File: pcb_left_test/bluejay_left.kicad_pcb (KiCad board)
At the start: 2 copper layers, 147 x 140.5 mm, 81 parts, among them J1 SJ-43514, U1 ATmega328P-PU, Y1 16MHz

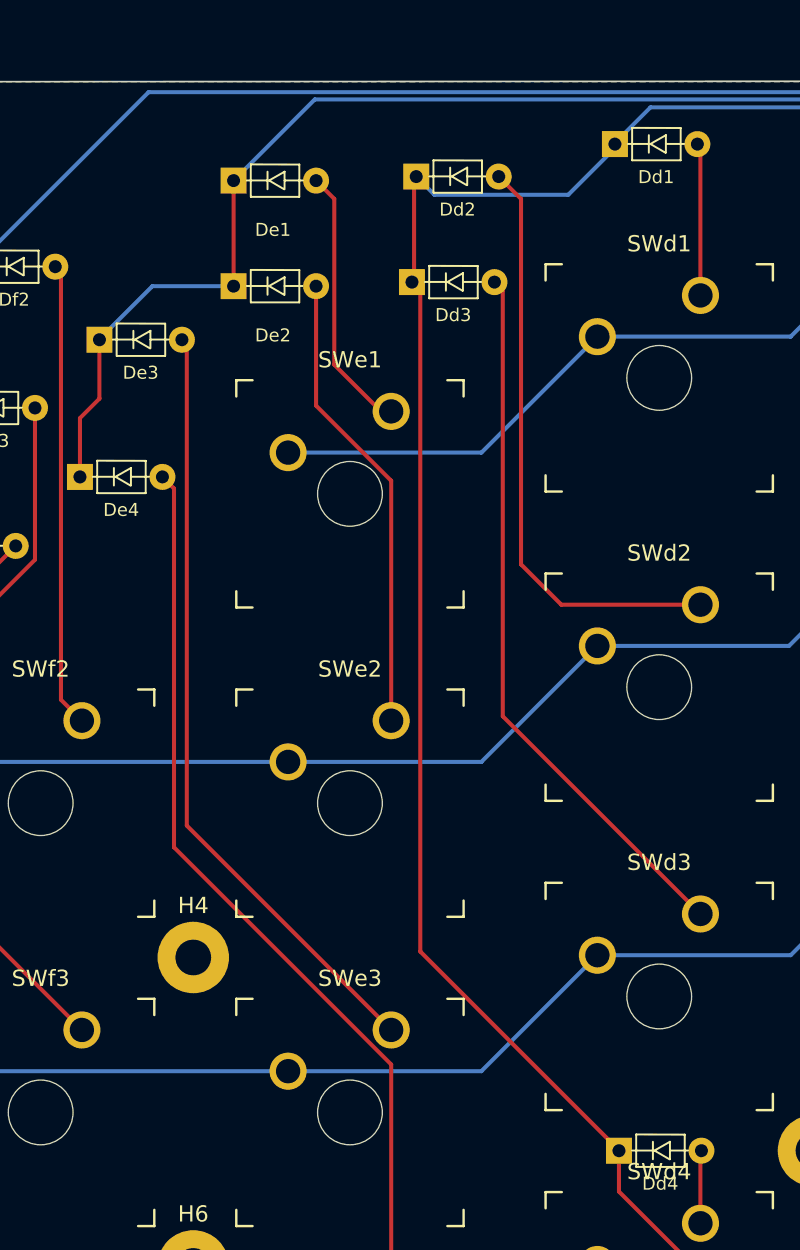
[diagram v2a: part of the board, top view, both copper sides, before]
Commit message: Fine tune placement of diodes
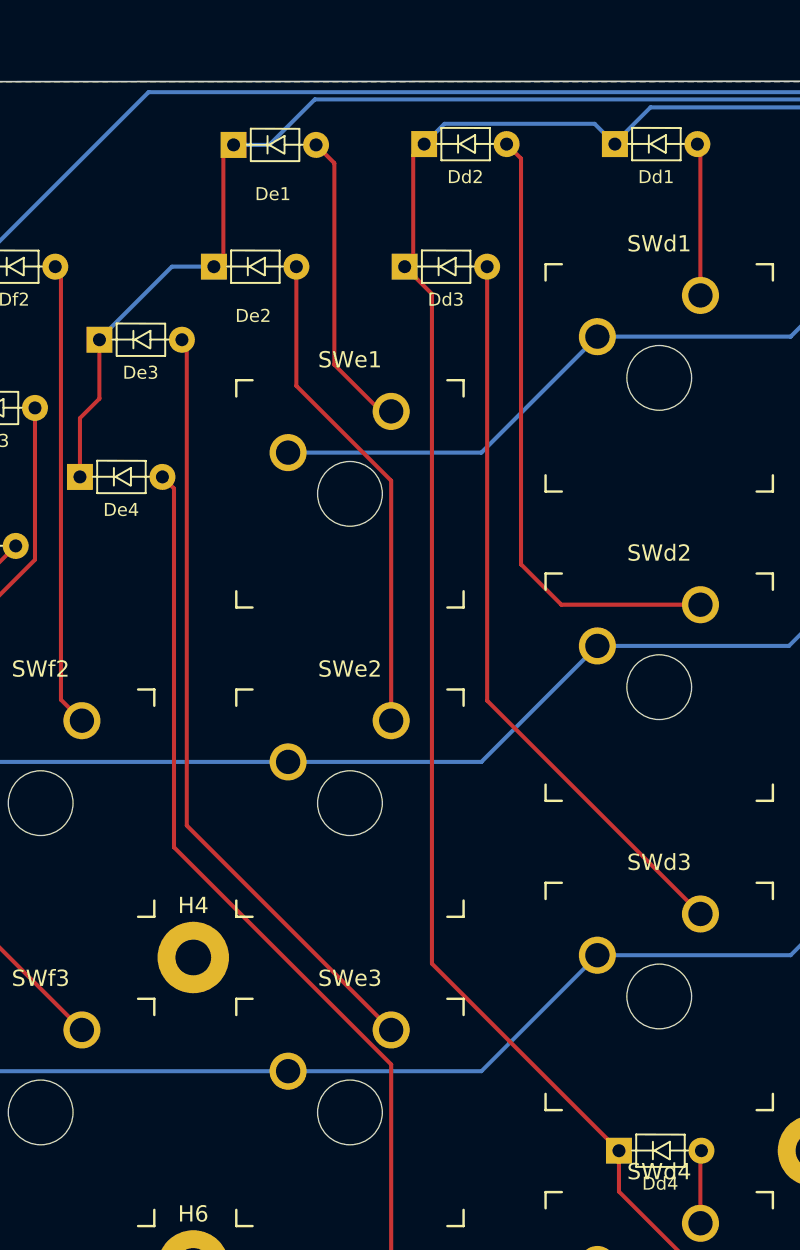
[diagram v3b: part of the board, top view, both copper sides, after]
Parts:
- moved De1 2.20 mm to (-65.6, -52.5)
- moved Dd2 2.06 mm to (-53.9, -52.5)
- moved De2 1.71 mm to (-66.8, -45.0)
- moved Dd3 1.05 mm to (-55.0, -45.0)
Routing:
- net Net-(De1-Pad2): track 16.5 -> 18.7 mm
- net Net-(Dd2-Pad2): track 36.5 -> 38.3 mm
- net Net-(De2-Pad2): track 28.7 -> 30.4 mm
- net /colD: track 228.3 -> 229.5 mm
- net Net-(Dd3-Pad2): track 44.2 -> 45.3 mm
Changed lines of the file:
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@@
   )
   (footprint "BlueJay footprints:D_DO-35_SOD27_P5.08mm_Horizontal" (layer "F.Cu")
-    (at -65.5875 -43.75)
+    (at -66.8 -44.95)
     (descr "Diode, DO-35_SOD27 series, Axial, Horizontal, pin pitch=7.62mm, , length*diameter=4*2mm^2, , http://www.diodes.com/_files/packages/DO-35.pdf")
     (tags "Diode DO-35_SOD27 series Axial Horizontal pin pitch 7.62mm  length 4mm diameter 2mm")
@@
   )
   (footprint "BlueJay footprints:D_DO-35_SOD27_P5.08mm_Horizontal" (layer "F.Cu")
-    (at -65.5875 -50.25)
+    (at -65.5875 -52.45)
     (descr "Diode, DO-35_SOD27 series, Axial, Horizontal, pin pitch=7.62mm, , length*diameter=4*2mm^2, , http://www.diodes.com/_files/packages/DO-35.pdf")
     (tags "Diode DO-35_SOD27 series Axial Horizontal pin pitch 7.62mm  length 4mm diameter 2mm")
@@
   )
   (footprint "BlueJay footprints:D_DO-35_SOD27_P5.08mm_Horizontal" (layer "F.Cu")
-    (at -54.3375 -50.5)
+    (at -53.85 -52.5)
     (descr "Diode, DO-35_SOD27 series, Axial, Horizontal, pin pitch=7.62mm, , length*diameter=4*2mm^2, , http://www.diodes.com/_files/packages/DO-35.pdf")
     (tags "Diode DO-35_SOD27 series Axial Horizontal pin pitch 7.62mm  length 4mm diameter 2mm")
@@
   )
   (footprint "BlueJay footprints:D_DO-35_SOD27_P5.08mm_Horizontal" (layer "F.Cu")
-    (at -54.6 -44)
+    (at -55.05 -44.95)
     (descr "Diode, DO-35_SOD27 series, Axial, Horizontal, pin pitch=7.62mm, , length*diameter=4*2mm^2, , http://www.diodes.com/_files/packages/DO-35.pdf")
     (tags "Diode DO-35_SOD27 series Axial Horizontal pin pitch 7.62mm  length 4mm diameter 2mm")
@@
   (segment (start -40.58 12.02) (end -40.58 9.5) (width 0.25) (layer "F.Cu") (net 23))
   (segment (start -22.1175 28.4) (end -24.2 28.4) (width 0.25) (layer "F.Cu") (net 23))
+  (segment (start -52.1 -43.27) (end -53.78 -44.95) (width 0.25) (layer "F.Cu") (net 23))
   (segment (start -24.2 28.4) (end -40.58 12.02) (width 0.25) (layer "F.Cu") (net 23))
-  (segment (start -40.58 9.47) (end -52.8175 -2.7675) (width 0.25) (layer "F.Cu") (net 23))
-  (segment (start -52.8175 -2.7675) (end -52.8175 -43.4875) (width 0.25) (layer "F.Cu") (net 23))
-  (segment (start -53.2 -50.3675) (end -53.0675 -50.5) (width 0.25) (layer "F.Cu") (net 23))
-  (segment (start -52.8175 -43.4875) (end -53.33 -44) (width 0.25) (layer "F.Cu") (net 23))
-  (segment (start -53.33 -44) (end -53.2 -44.13) (width 0.25) (layer "F.Cu") (net 23))
+  (segment (start -40.58 9.5) (end -52.1 -2.02) (width 0.25) (layer "F.Cu") (net 23))
+  (segment (start -52.1 -2.02) (end -52.1 -43.27) (width 0.25) (layer "F.Cu") (net 23))
+  (segment (start -53.25 -45.48) (end -53.25 -51.83) (width 0.25) (layer "F.Cu") (net 23))
+  (segment (start -53.78 -44.95) (end -53.25 -45.48) (width 0.25) (layer "F.Cu") (net 23))
   (segment (start 55.2755 -19.1418) (end 53.5512 -17.4175) (width 0.25) (layer "F.Cu") (net 23))
-  (segment (start -40.58 9.5) (end -40.58 9.47) (width 0.25) (layer "F.Cu") (net 23))
-  (segment (start -53.2 -44.13) (end -53.2 -50.3675) (width 0.25) (layer "F.Cu") (net 23))
+  (segment (start -53.25 -51.83) (end -52.58 -52.5) (width 0.25) (layer "F.Cu") (net 23))
   (via (at 55.2755 -30.550989) (size 0.8) (drill 0.4) (layers "F.Cu" "B.Cu") (net 23))
+  (segment (start -51.33 -53.75) (end -42.08 -53.75) (width 0.25) (layer "B.Cu") (net 23))
   (segment (start 54.726489 -31.1) (end 55.2755 -30.550989) (width 0.25) (layer "B.Cu") (net 23))
+  (segment (start -42.08 -53.75) (end -40.83 -52.5) (width 0.25) (layer "B.Cu") (net 23))
   (segment (start 38.2 -31.1) (end 54.726489 -31.1) (width 0.25) (layer "B.Cu") (net 23))
-  (segment (start -51.942989 -49.375489) (end -43.704511 -49.375489) (width 0.25) (layer "B.Cu") (net 23))
   (segment (start -38.635718 -54.764282) (end 14.535718 -54.764282) (width 0.25) (layer "B.Cu") (net 23))
-  (segment (start -43.704511 -49.375489) (end -40.83 -52.25) (width 0.25) (layer "B.Cu") (net 23))
+  (segment (start -52.58 -52.5) (end -51.33 -53.75) (width 0.25) (layer "B.Cu") (net 23))
   (segment (start -40.83 -52.57) (end -38.635718 -54.764282) (width 0.25) (layer "B.Cu") (net 23))
   (segment (start 14.535718 -54.764282) (end 38.2 -31.1) (width 0.25) (layer "B.Cu") (net 23))
-  (segment (start -40.83 -52.25) (end -40.83 -52.5) (width 0.25) (layer "B.Cu") (net 23))
-  (segment (start -53.0675 -50.5) (end -51.942989 -49.375489) (width 0.25) (layer "B.Cu") (net 23))
   (segment (start -40.83 -52.5) (end -40.83 -52.57) (width 0.25) (layer "B.Cu") (net 23))
   (segment (start -35.56 -52.31) (end -35.75 -52.5) (width 0.25) (layer "F.Cu") (net 24))
   (segment (start -35.56 -43.18) (end -35.56 -52.31) (width 0.25) (layer "F.Cu") (net 24))
-  (segment (start -44.13 -24.13) (end -46.612989 -26.612989) (width 0.25) (layer "F.Cu") (net 25))
   (segment (start -35.56 -24.13) (end -44.13 -24.13) (width 0.25) (layer "F.Cu") (net 25))
-  (segment (start -46.612989 -26.612989) (end -46.612989 -49.125489) (width 0.25) (layer "F.Cu") (net 25))
-  (segment (start -46.612989 -49.125489) (end -47.9875 -50.5) (width 0.25) (layer "F.Cu") (net 25))
-  (segment (start -47.7375 -43.4875) (end -48.25 -44) (width 0.25) (layer "F.Cu") (net 26))
-  (segment (start -35.56 -5.08) (end -47.7375 -17.2575) (width 0.25) (layer "F.Cu") (net 26))
-  (segment (start -47.7375 -17.2575) (end -47.7375 -43.4875) (width 0.25) (layer "F.Cu") (net 26))
+  (segment (start -46.612989 -51.612989) (end -47.5 -52.5) (width 0.25) (layer "F.Cu") (net 25))
+  (segment (start -46.612989 -26.612989) (end -46.612989 -51.612989) (width 0.25) (layer "F.Cu") (net 25))
+  (segment (start -44.13 -24.13) (end -46.612989 -26.612989) (width 0.25) (layer "F.Cu") (net 25))
+  (segment (start -48.7 -18.22) (end -48.7 -44.95) (width 0.25) (layer "F.Cu") (net 26))
+  (segment (start -35.56 -5.08) (end -48.7 -18.22) (width 0.25) (layer "F.Cu") (net 26))
   (segment (start -35.56 13.97) (end -35.56 9.56) (width 0.25) (layer "F.Cu") (net 27))
   (segment (start -35.56 9.56) (end -35.5 9.5) (width 0.25) (layer "F.Cu") (net 27))
   (segment (start -6.985 40.1638) (end -6.985 38.4525) (width 0.25) (layer "F.Cu") (net 28))
   (segment (start -6.985 38.4525) (end -17.0375 28.4) (width 0.25) (layer "F.Cu") (net 28))
+  (segment (start -64.95 -45.53) (end -64.95 -51.8175) (width 0.25) (layer "F.Cu") (net 29))
   (segment (start 56 -31.243596) (end 56 -17.3263) (width 0.25) (layer "F.Cu") (net 29))
   (segment (start 56 -17.3263) (end 53.5512 -14.8775) (width 0.25) (layer "F.Cu") (net 29))
+  (segment (start -64.95 -51.8175) (end -64.3175 -52.45) (width 0.25) (layer "F.Cu") (net 29))
+  (segment (start -65.53 -44.95) (end -64.95 -45.53) (width 0.25) (layer "F.Cu") (net 29))
   (segment (start -73.78 -32) (end -73.78 -35.62) (width 0.25) (layer "F.Cu") (net 29))
-  (segment (start -64.3175 -43.75) (end -64.3175 -50.25) (width 0.25) (layer "F.Cu") (net 29))
   (segment (start 56.031904 -31.2755) (end 56 -31.243596) (width 0.25) (layer "F.Cu") (net 29))
   (segment (start -72.58 -36.82) (end -72.58 -40.45) (width 0.25) (layer "F.Cu") (net 29))
   (segment (start -73.78 -35.62) (end -72.58 -36.82) (width 0.25) (layer "F.Cu") (net 29))
   (via (at 56.031904 -31.2755) (size 0.8) (drill 0.4) (layers "F.Cu" "B.Cu") (net 29))
+  (segment (start -68.1175 -44.95) (end -65.53 -44.95) (width 0.25) (layer "B.Cu") (net 29))
   (segment (start -72.58 -40.45) (end -72.58 -40.4875) (width 0.25) (layer "B.Cu") (net 29))
-  (segment (start -72.58 -40.4875) (end -69.3175 -43.75) (width 0.25) (layer "B.Cu") (net 29))
-  (segment (start -69.3175 -43.75) (end -64.3175 -43.75) (width 0.25) (layer "B.Cu") (net 29))
-  (segment (start -64.3175 -50.25) (end -59.31702 -55.25048) (width 0.25) (layer "B.Cu") (net 29))
+  (segment (start -62.1175 -52.45) (end -59.31702 -55.25048) (width 0.25) (layer "B.Cu") (net 29))
+  (segment (start 14.713802 -55.25048) (end 38.164282 -31.8) (width 0.25) (layer "B.Cu") (net 29))
   (segment (start 55.507404 -31.8) (end 56.031904 -31.2755) (width 0.25) (layer "B.Cu") (net 29))
-  (segment (start 38.164282 -31.8) (end 55.507404 -31.8) (width 0.25) (layer "B.Cu") (net 29))
+  (segment (start -72.58 -40.4875) (end -68.1175 -44.95) (width 0.25) (layer "B.Cu") (net 29))
   (segment (start -59.31702 -55.25048) (end 14.713802 -55.25048) (width 0.25) (layer "B.Cu") (net 29))
-  (segment (start 14.713802 -55.25048) (end 38.164282 -31.8) (width 0.25) (layer "B.Cu") (net 29))
+  (segment (start -64.3175 -52.45) (end -62.1175 -52.45) (width 0.25) (layer "B.Cu") (net 29))
+  (segment (start 38.164282 -31.8) (end 55.507404 -31.8) (width 0.25) (layer "B.Cu") (net 29))
   (segment (start -54.61 -36.0363) (end -55.2363 -36.0363) (width 0.25) (layer "F.Cu") (net 30))
-  (segment (start -58.112989 -49.125489) (end -59.2375 -50.25) (width 0.25) (layer "F.Cu") (net 30))
-  (segment (start -58.112989 -38.912989) (end -58.112989 -49.125489) (width 0.25) (layer "F.Cu") (net 30))
+  (segment (start -58.112989 -38.912989) (end -58.112989 -51.325489) (width 0.25) (layer "F.Cu") (net 30))
   (segment (start -55.2363 -36.0363) (end -58.112989 -38.912989) (width 0.25) (layer "F.Cu") (net 30))
-  (segment (start -59.2375 -36.393254) (end -59.2375 -43.75) (width 0.25) (layer "F.Cu") (net 31))
-  (segment (start -54.61 -31.765754) (end -59.2375 -36.393254) (width 0.25) (layer "F.Cu") (net 31))
+  (segment (start -58.112989 -51.325489) (end -59.2375 -52.45) (width 0.25) (layer "F.Cu") (net 30))
+  (segment (start -54.61 -31.765754) (end -60.45 -37.605754) (width 0.25) (layer "F.Cu") (net 31))
   (segment (start -54.61 -16.9863) (end -54.61 -31.765754) (width 0.25) (layer "F.Cu") (net 31))
+  (segment (start -60.45 -37.605754) (end -60.45 -44.95) (width 0.25) (layer "F.Cu") (net 31))
   (segment (start -67.2 -10.5262) (end -67.2 -40.15) (width 0.25) (layer "F.Cu") (net 32))
   (segment (start -67.2 -40.15) (end -67.5 -40.45) (width 0.25) (layer "F.Cu") (net 32))

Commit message: Complete alternative version of pcbs
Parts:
- moved H9 2.26 mm to (57.0, 64.2)
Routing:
- net GND: vias 2 -> 4
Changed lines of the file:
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@@
   )
   (footprint "MountingHole:MountingHole_2.2mm_M2_Pad" (layer "F.Cu")
-    (at 57.2 66.4)
+    (at 56.95 64.15)
     (descr "Mounting Hole 2.2mm, M2")
     (tags "mounting hole 2.2mm m2")
@@
   (gr_line (start 39.85 -56.4) (end -84.024489 -56.3437) (layer "Edge.Cuts") (width 0.1))
   (gr_arc (start 49.7812 83.7263) (mid 48.888799 84.147698) (end 48.0112 83.6963) (layer "Edge.Cuts") (width 0.1))
-  (via (at 36.35 -49.15) (size 0.8) (drill 0.4) (layers "F.Cu" "B.Cu") (free) (net 1))
-  (via (at 36.4 -44.45) (size 0.8) (drill 0.4) (layers "F.Cu" "B.Cu") (free) (net 1))
+  (via (at 36.5 -49.2) (size 0.8) (drill 0.4) (layers "F.Cu" "B.Cu") (free) (net 1))
+  (via (at 37.6 -43.3) (size 0.8) (drill 0.4) (layers "F.Cu" "B.Cu") (free) (net 1))
+  (via (at 35.1 -49.25) (size 0.8) (drill 0.4) (layers "F.Cu" "B.Cu") (free) (net 1))
+  (via (at 36.2 -44.55) (size 0.8) (drill 0.4) (layers "F.Cu" "B.Cu") (free) (net 1))
   (segment (start 42.7874 -4.7175) (end 45.9312 -4.7175) (width 0.25) (layer "F.Cu") (net 2))
   (segment (start 41.4812 -10.0937) (end 40.7312 -10.8437) (width 0.25) (layer "F.Cu") (net 2))
@@
   (segment (start -73.66 21.1138) (end -81.927021 12.846779) (width 0.25) (layer "F.Cu") (net 37))
   (segment (start -81.927021 -23.560479) (end -77.7375 -27.75) (width 0.25) (layer "F.Cu") (net 37))
-  (segment (start 38.959511 -43.840489) (end 38.959511 -21.399511) (width 0.2) (layer "F.Cu") (net 38))
-  (segment (start 30.9312 -48.4437) (end 30.9312 -48.595102) (width 0.2) (layer "F.Cu") (net 38))
-  (segment (start 30.9312 -48.595102) (end 32.179318 -49.84322) (width 0.2) (layer "F.Cu") (net 38))
-  (segment (start 38.959511 -21.399511) (end 37.96 -20.4) (width 0.2) (layer "F.Cu") (net 38))
-  (segment (start 32.95678 -49.84322) (end 38.959511 -43.840489) (width 0.2) (layer "F.Cu") (net 38))
-  (segment (start 32.179318 -49.84322) (end 32.95678 -49.84322) (width 0.2) (layer "F.Cu") (net 38))
-  (segment (start 30.5924 -48.7825) (end 30.9312 -48.4437) (width 0.2) (layer "B.Cu") (net 38))
-  (segment (start 30.9312 -48.4437) (end 30.9312 -48.595102) (width 0.2) (layer "B.Cu") (net 38))
-  (segment (start 30.9312 -48.595102) (end 32.686098 -50.35) (width 0.2) (layer "B.Cu") (net 38))
-  (segment (start 40.9812 -53.2312) (end 40.9812 -53.75) (width 0.2) (layer "B.Cu") (net 38))
-  (segment (start 25 -48.7825) (end 30.5924 -48.7825) (width 0.2) (layer "B.Cu") (net 38))
-  (segment (start 38.1 -50.35) (end 40.9812 -53.2312) (width 0.2) (layer "B.Cu") (net 38))
-  (segment (start 32.686098 -50.35) (end 38.1 -50.35) (width 0.2) (layer "B.Cu") (net 38))
-  (segment (start 37.96 -40.863498) (end 37.96 -22.6) (width 0.2) (layer "F.Cu") (net 39))
-  (segment (start 31.7312 -47.2437) (end 31.7312 -47.092298) (width 0.2) (layer "F.Cu") (net 39))
-  (segment (start 31.7312 -47.092298) (end 37.96 -40.863498) (width 0.2) (layer "F.Cu") (net 39))
-  (segment (start 35.56168 -45.84418) (end 38.3 -48.5825) (width 0.2) (layer "B.Cu") (net 39))
-  (segment (start 31.7312 -47.092298) (end 32.979318 -45.84418) (width 0.2) (layer "B.Cu") (net 39))
-  (segment (start 32.979318 -45.84418) (end 35.56168 -45.84418) (width 0.2) (layer "B.Cu") (net 39))
-  (segment (start 31.7312 -47.2437) (end 31.7312 -47.092298) (width 0.2) (layer "B.Cu") (net 39))
+  (segment (start 30.9312 -48.630458) (end 32.168962 -49.86822) (width 0.25) (layer "F.Cu") (net 38))
+  (segment (start 39 -43.8) (end 39 -21.44) (width 0.25) (layer "F.Cu") (net 38))
+  (segment (start 30.9312 -48.4437) (end 30.9312 -48.630458) (width 0.25) (layer "F.Cu") (net 38))
+  (segment (start 32.93178 -49.86822) (end 39 -43.8) (width 0.25) (layer "F.Cu") (net 38))
+  (segment (start 39 -21.44) (end 37.96 -20.4) (width 0.25) (layer "F.Cu") (net 38))
+  (segment (start 32.168962 -49.86822) (end 32.93178 -49.86822) (width 0.25) (layer "F.Cu") (net 38))
+  (segment (start 30.9312 -48.630458) (end 32.168962 -49.86822) (width 0.25) (layer "B.Cu") (net 38))
+  (segment (start 30.9312 -48.4437) (end 30.9312 -48.630458) (width 0.25) (layer "B.Cu") (net 38))
+  (segment (start 30.5924 -48.7825) (end 30.9312 -48.4437) (width 0.25) (layer "B.Cu") (net 38))
+  (segment (start 32.7 -50.35) (end 37.5812 -50.35) (width 0.25) (layer "B.Cu") (net 38))
+  (segment (start 32.168962 -49.86822) (end 32.21822 -49.86822) (width 0.25) (layer "B.Cu") (net 38))
+  (segment (start 32.21822 -49.86822) (end 32.7 -50.35) (width 0.25) (layer "B.Cu") (net 38))
+  (segment (start 25 -48.7825) (end 30.5924 -48.7825) (width 0.25) (layer "B.Cu") (net 38))
+  (segment (start 37.5812 -50.35) (end 40.9812 -53.75) (width 0.25) (layer "B.Cu") (net 38))
+  (segment (start 37.96 -40.84) (end 37.96 -22.6) (width 0.25) (layer "F.Cu") (net 39))
+  (segment (start 32.98082 -45.81918) (end 37.96 -40.84) (width 0.25) (layer "F.Cu") (net 39))
+  (segment (start 31.7312 -47.2437) (end 31.7312 -47.056942) (width 0.25) (layer "F.Cu") (net 39))
+  (segment (start 31.7312 -47.056942) (end 32.968962 -45.81918) (width 0.25) (layer "F.Cu") (net 39))
+  (segment (start 32.968962 -45.81918) (end 32.98082 -45.81918) (width 0.25) (layer "F.Cu") (net 39))
+  (segment (start 35.53668 -45.81918) (end 38.3 -48.5825) (width 0.25) (layer "B.Cu") (net 39))
+  (segment (start 31.7312 -47.2437) (end 31.7312 -47.056942) (width 0.25) (layer "B.Cu") (net 39))
+  (segment (start 31.7312 -47.056942) (end 32.968962 -45.81918) (width 0.25) (layer "B.Cu") (net 39))
+  (segment (start 32.968962 -45.81918) (end 35.53668 -45.81918) (width 0.25) (layer "B.Cu") (net 39))
   (segment (start 30.1312 -47.2437) (end 30.1312 -46.950876) (width 0.4) (layer "B.Cu") (net 40))
   (segment (start 35.138376 -41.9437) (end 42.4312 -41.9437) (width 0.4) (layer "B.Cu") (net 40))
@@
   (segment (start 47.055711 -23.912989) (end 45.9312 -25.0375) (width 0.25) (layer "B.Cu") (net 43))
   (segment (start 58.8 -23.9) (end 57.812989 -23.912989) (width 0.25) (layer "B.Cu") (net 43))
-  (segment (start 43.04 -20.4) (end 44.831689 -18.608311) (width 0.2) (layer "F.Cu") (net 44))
-  (segment (start 44.831689 -16.868311) (end 45.9312 -15.7688) (width 0.2) (layer "F.Cu") (net 44))
-  (segment (start 45.9312 -15.7688) (end 45.9312 -14.8775) (width 0.2) (layer "F.Cu") (net 44))
-  (segment (start 44.831689 -18.608311) (end 44.831689 -16.868311) (width 0.2) (layer "F.Cu") (net 44))
-  (segment (start 45.9312 -18.073806) (end 45.9312 -17.4175) (width 0.2) (layer "F.Cu") (net 45))
-  (segment (start 44.039511 -19.985988) (end 44.029265 -19.975741) (width 0.2) (layer "F.Cu") (net 45))
-  (segment (start 44.029265 -19.975741) (end 45.9312 -18.073806) (width 0.2) (layer "F.Cu") (net 45))
-  (segment (start 43.04 -22.6) (end 44.039511 -21.600489) (width 0.2) (layer "F.Cu") (net 45))
-  (segment (start 44.039511 -21.600489) (end 44.039511 -19.985988) (width 0.2) (layer "F.Cu") (net 45))
+  (segment (start 44.806689 -16.002011) (end 45.9312 -14.8775) (width 0.25) (layer "F.Cu") (net 44))
+  (segment (start 43.04 -20.4) (end 43.04 -20.16) (width 0.25) (layer "F.Cu") (net 44))
+  (segment (start 43.04 -20.16) (end 44.806689 -18.393311) (width 0.25) (layer "F.Cu") (net 44))
+  (segment (start 44.806689 -18.393311) (end 44.806689 -16.002011) (width 0.25) (layer "F.Cu") (net 44))
+  (segment (start 45.9312 -18.3188) (end 45.9312 -17.4175) (width 0.25) (layer "F.Cu") (net 45))
+  (segment (start 44.151762 -20.098238) (end 45.9312 -18.3188) (width 0.25) (layer "F.Cu") (net 45))
+  (segment (start 43.04 -22.6) (end 44.151762 -21.488238) (width 0.25) (layer "F.Cu") (net 45))
+  (segment (start 44.151762 -21.488238) (end 44.151762 -20.098238) (width 0.25) (layer "F.Cu") (net 45))
   (segment (start 59.516988 7.883012) (end 59.516988 -21.498695) (width 0.25) (layer "F.Cu") (net 46))
   (segment (start 57.175489 20.074511) (end 57.175489 10.224511) (width 0.25) (layer "F.Cu") (net 46))
